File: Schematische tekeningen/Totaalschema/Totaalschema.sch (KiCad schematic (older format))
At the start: 24 parts

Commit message: Footprints toegevoegd en toegewezen. Tekening weer iets aangepast
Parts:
- removed D?: LED, symbol Device:LED
- removed Q?: Q_Photo_NPN, symbol Device:Q_Photo_NPN
- removed R?: 1k, symbol Device:R_Small
- added J10: ALL GPIO_1, Connector_PinHeader_2.54mm:PinHeader_1x20_P2.54mm_Vertical, symbol Connector:Conn_01x20_Male
- added J11: ALL GPIO_2, Connector_PinHeader_2.54mm:PinHeader_1x20_P2.54mm_Vertical, symbol Connector:Conn_01x20_Male
- added J12: 3.3V pwr, Connector_PinHeader_2.54mm:PinHeader_2x06_P2.54mm_Vertical, symbol Connector_Generic:Conn_02x06_Top_Bottom
- added R3: 1k, Resistor_SMD:R_0603_1608Metric_Pad0.98x0.95mm_HandSolder, symbol Device:R_Small
- added U14: Snelheidssensor, Connector_PinHeader_2.54mm:PinHeader_1x04_P2.54mm_Vertical, symbol eec:Snelheidssensor
- C1, C2, C3, C4: renamed from C?; footprint (none) -> Capacitor_SMD:C_0603_1608Metric_Pad1.08x0.95mm_HandSolder
- IC1: renamed from IC?; footprint QFP50P900X900X160-48N -> eec:QFP50P900X900X160-48N
- J1: renamed from J?; footprint (none) -> Connector_PinHeader_2.54mm:PinHeader_1x04_P2.54mm_Vertical
- J2, J3, J5, J6: renamed from J?; footprint (none) -> TestPoint:TestPoint_Plated_Hole_D2.0mm
- J4: renamed from J?; footprint (none) -> Connector_PinHeader_2.54mm:PinHeader_1x08_P2.54mm_Vertical
- J7: renamed from J?; value Conn_01x12_Male -> Breakoutbord; footprint (none) -> Connector_PinHeader_2.54mm:PinHeader_1x12_P2.54mm_Vertical
- R1, R2, R4: renamed from R?; footprint (none) -> Resistor_SMD:R_0603_1608Metric_Pad0.98x0.95mm_HandSolder
- SW1: renamed from SW?; footprint (none) -> Button_Switch_SMD:SW_SPST_EVPBF
- U1: renamed from U?; footprint (none) -> Package_SO:SO-14_3.9x8.65mm_P1.27mm
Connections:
- net labels added: Noodstop_ext, P1.0, P1.1, P1.2, P2.5, P2.6, P3.1, P3.4, P3.5, P3.7, P4.1, P4.2, P4.3, P4.4, P4.5, P4.7, P5.4, P5.6, P5.7, P6.0, P6.1, P6.2
- wire segments 41 -> 49
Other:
- moved on the sheet: J2, J3, J5, J6, R2, U1A, U1B, U1C, U1D

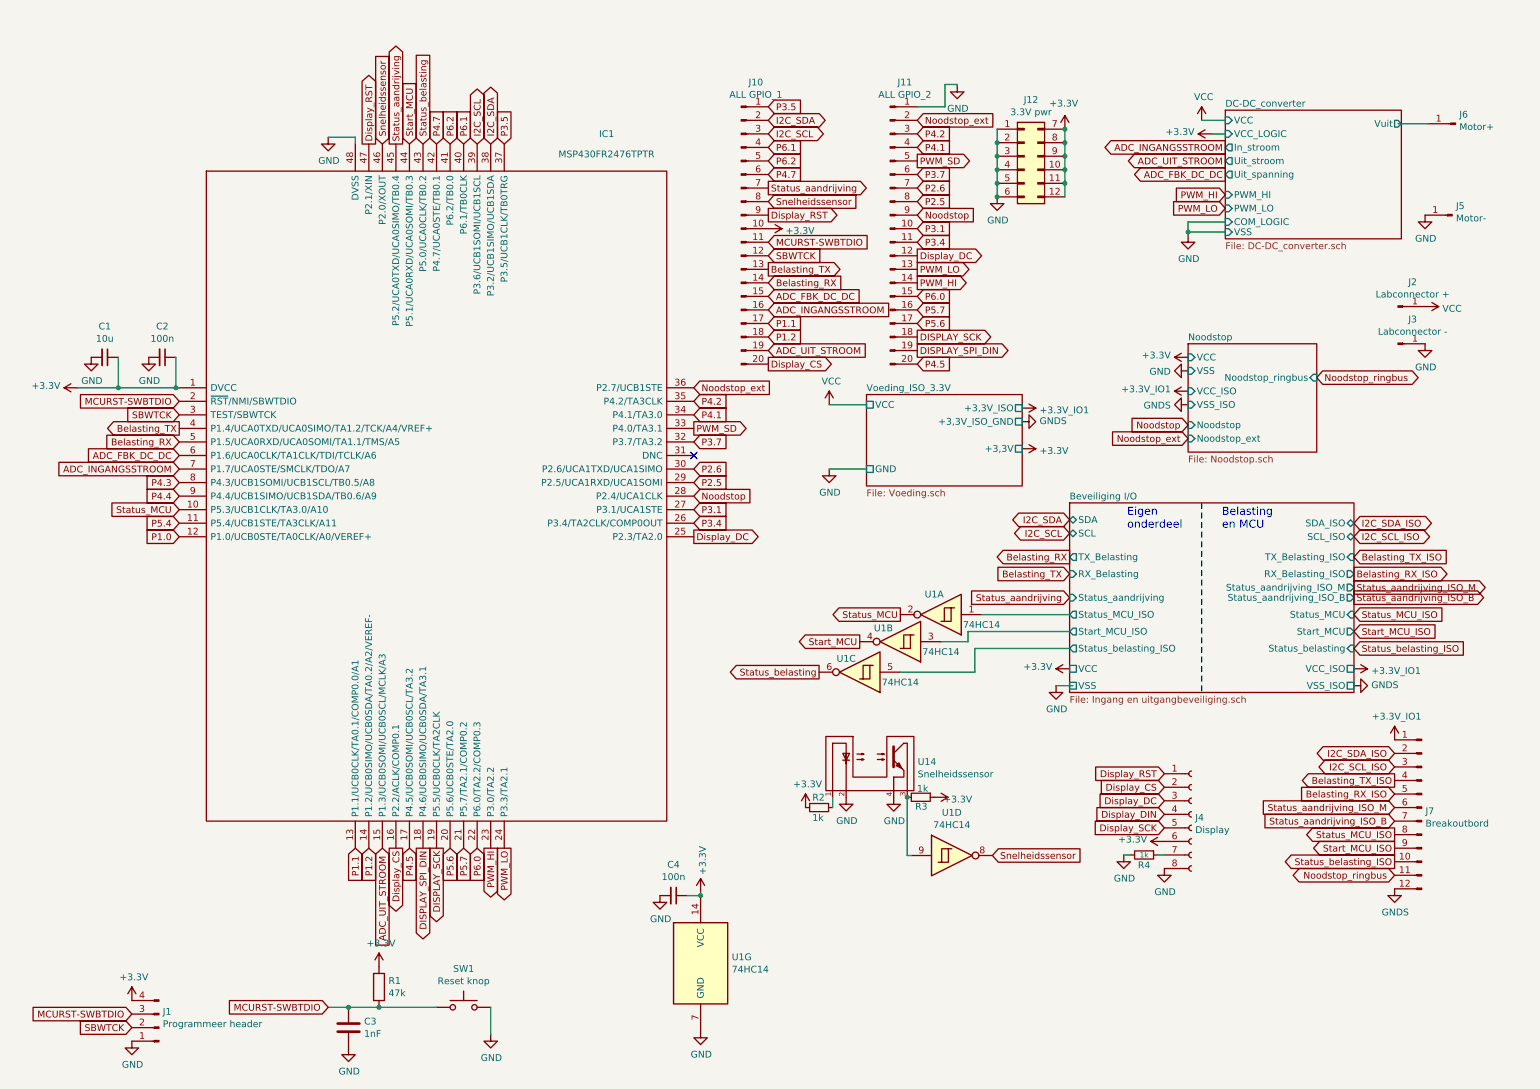
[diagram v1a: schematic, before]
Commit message: Footprints aangepast. Tekening aangepast
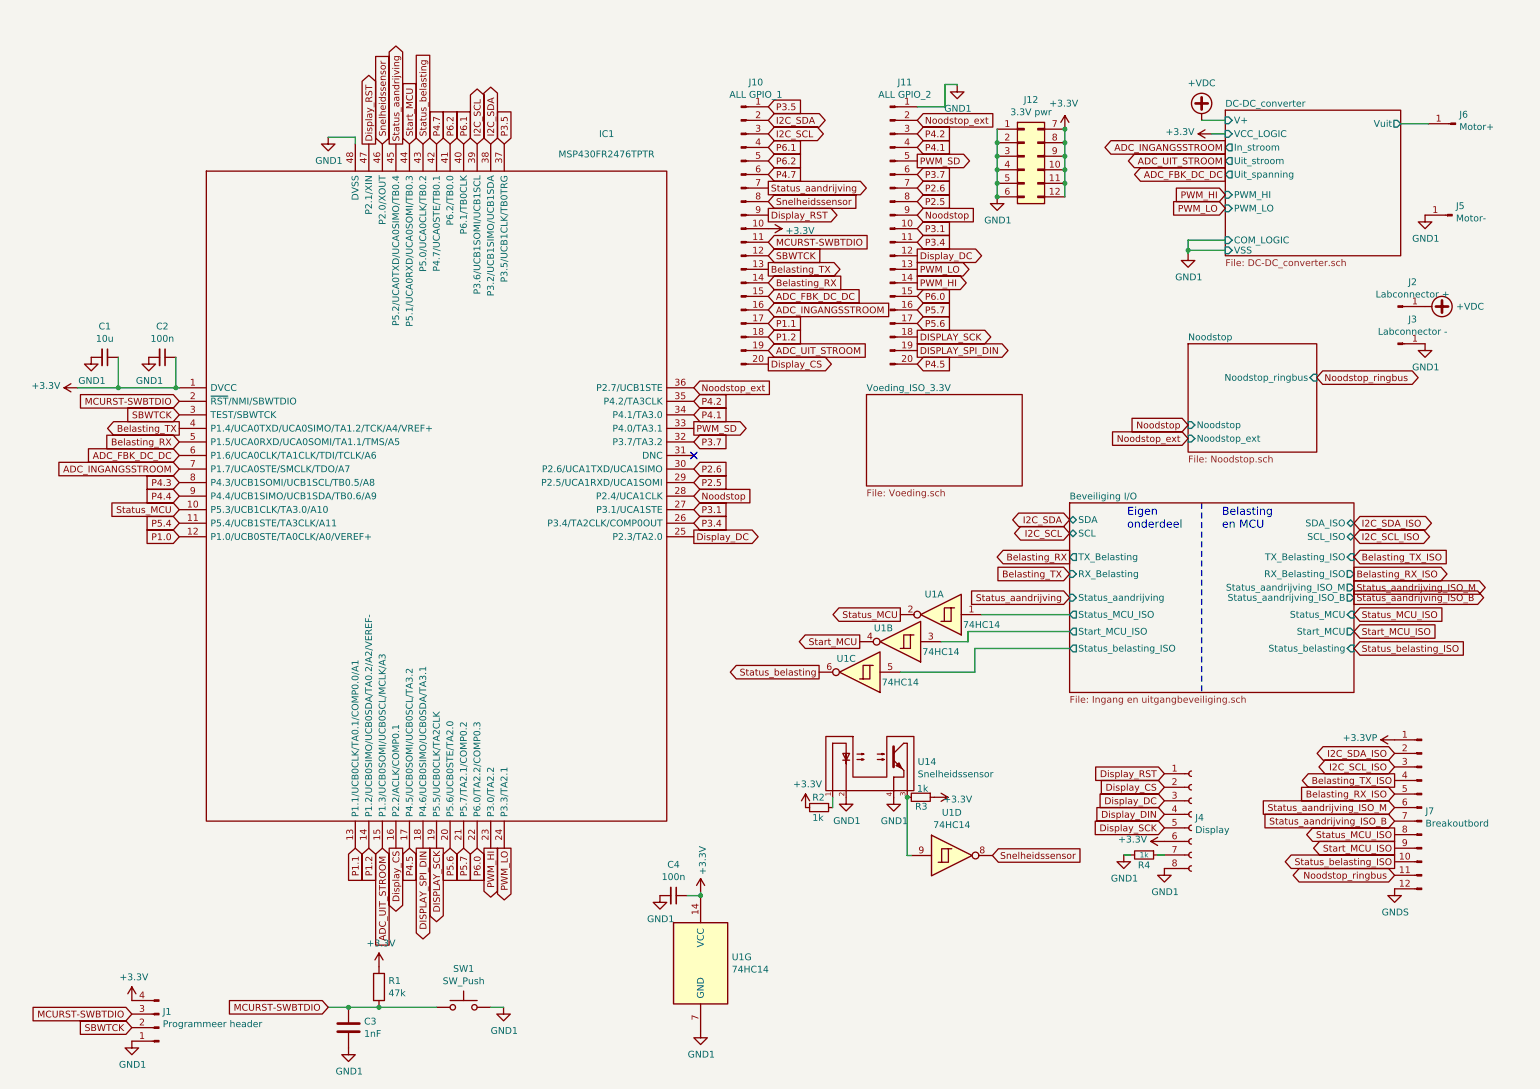
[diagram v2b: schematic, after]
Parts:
- J10, J11: footprint Connector_PinHeader_2.54mm:PinHeader_1x20_P2.54mm_Vertical -> Connector_PinHeader_2.54mm:PinHeader_2x10_P2.54mm_Vertical_SMD
- J12: footprint Connector_PinHeader_2.54mm:PinHeader_2x06_P2.54mm_Vertical -> Connector_PinHeader_2.54mm:PinHeader_2x06_P2.54mm_Vertical_SMD
- SW1: value Reset knop -> SW_Push
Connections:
- net labels added: +3.3VP, +VDC, GND1
- net labels removed: +3.3V_IO1, GND, VCC
- wire segments 49 -> 46
